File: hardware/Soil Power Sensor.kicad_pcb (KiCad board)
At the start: 2 copper layers, 139 x 45 mm, 72 parts, among them J1 Screw_Terminal_01x05, J2 RFShield_OnePiece, J3 Debug, J4 Conn_01x03, J5 Micro_SD_Card, J7 Conn_01x04_Socket, J8 Conn_01x10, J9 Rsense, Q1 BSS123, Q2 L8050QLT1G, Q3 L8050QLT1G, SW1 BOOT, SW2 EN, SW3 SW_SPDT, U1 MAX9944, U10 Wio-E5 mini, U11 MB85RC1MT, U12 MB85RC1MT, U2 INA296A, U3 REF2033, U4 THS4532, U5 TPS60400DBV, U6 ADS1219, U7 SN74LVC1G240, U8 ESP32-C3-WROOM-02-N4

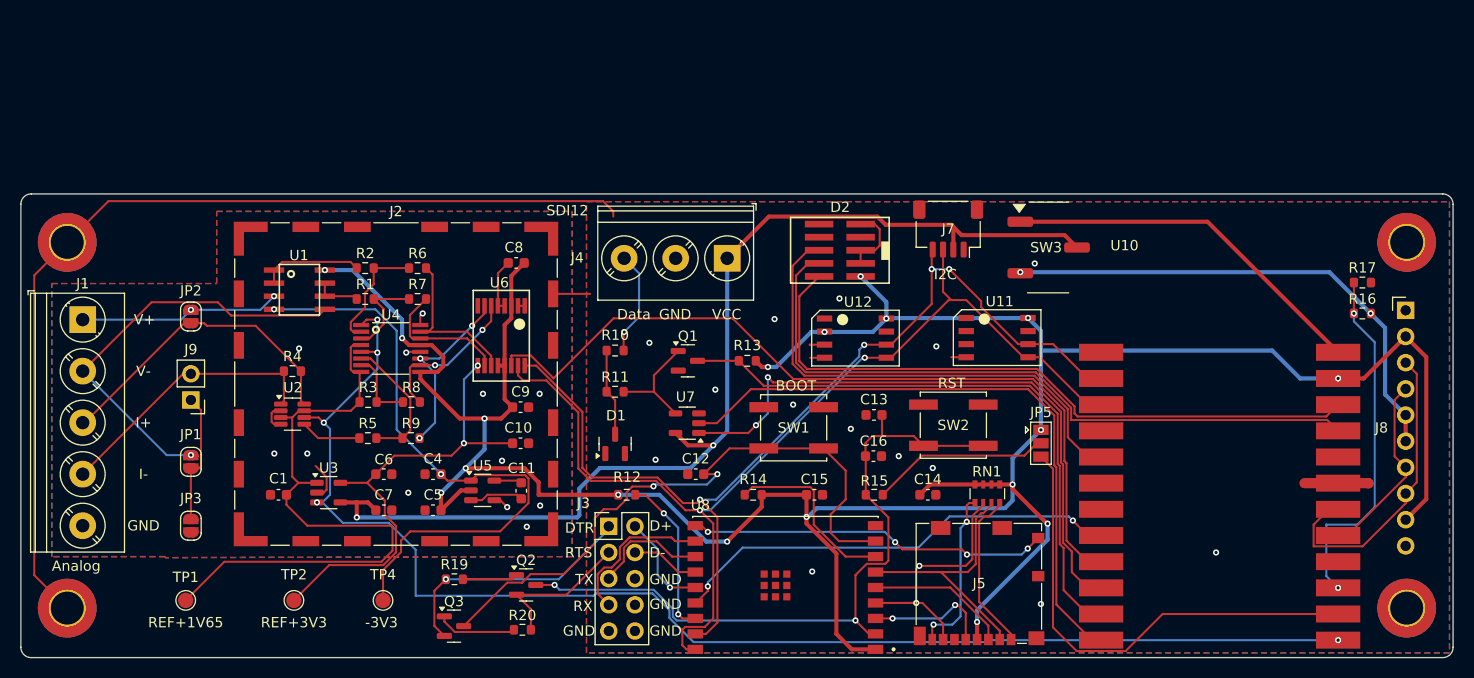
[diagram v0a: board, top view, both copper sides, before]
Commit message: replace mini with module
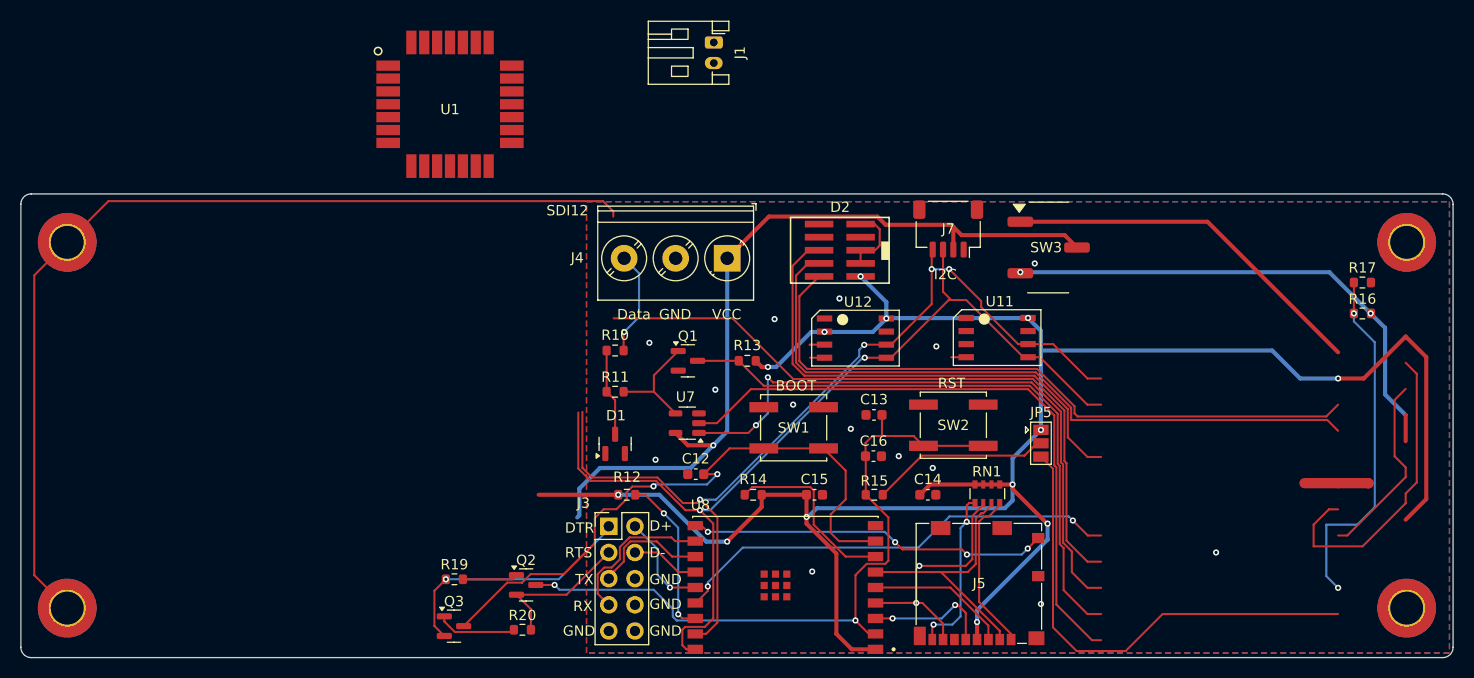
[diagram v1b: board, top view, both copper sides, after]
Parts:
- removed C1, C10, C6, C7, C8, C9: 0.1uF, Capacitor_SMD:C_0603_1608Metric
- removed C11, C4, C5: 1uF, Capacitor_SMD:C_0603_1608Metric
- removed J2: RFShield_OnePiece, RF_Shielding:Wuerth_36103305_30x30mm
- removed J8: Conn_01x10, Connector_PinHeader_2.54mm:PinHeader_1x10_P2.54mm_Horizontal
- removed J9: Rsense, Connector_PinHeader_2.54mm:PinHeader_1x02_P2.54mm_Vertical
- removed JP1, JP2, JP3: SolderJumper_2_Open, Jumper:SolderJumper-2_P1.3mm_Open_RoundedPad1.0x1.5mm
- removed R1, R2, R6, R7: 100k, Resistor_SMD:R_0603_1608Metric
- removed R3, R5: 10k, Resistor_SMD:R_0603_1608Metric
- removed R4: 330m, Resistor_SMD:R_0603_1608Metric
- removed R8, R9: 499k, Resistor_SMD:R_0603_1608Metric
- removed TP1: REF+1V65, TestPoint:TestPoint_Pad_D1.5mm
- removed TP2: REF+3V3, TestPoint:TestPoint_Pad_D1.5mm
- removed TP4: -3V3, TestPoint:TestPoint_Pad_D1.5mm
- removed U10: Wio-E5 mini, Soil Power Sensor:WIO-E5_MINI
- removed U2: INA296A, Package_TO_SOT_SMD:SOT-23-8
- removed U3: REF2033, Package_TO_SOT_SMD:SOT-23-5
- removed U4: THS4532, Soil Power Sensor:SOP65P640X120-16N
- removed U5: TPS60400DBV, Package_TO_SOT_SMD:SOT-23-5
- removed U6: ADS1219, Soil Power Sensor:TSSOP65P640X120-16
- J1: value Screw_Terminal_01x05 -> Conn_01x02; footprint TerminalBlock_Phoenix:TerminalBlock_Phoenix_PT-1,5-5-5.0-H_1x05_P5.00mm_Horizontal -> Connector_JST:JST_PH_S2B-PH-K_1x02_P2.00mm_Horizontal
- U1: value MAX9944 -> LoRa-E5; footprint Soil Power Sensor:SOIC127P600X155-8N -> Soil Power Sensor:LoRa-E5
- moved J1 66.9 mm to (179.2, 32.1)
- moved U1 23.2 mm to (153.7, 38.1)
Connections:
- J1 pad 1: /Analog/V+ -> /Power/VBAT
- J1 pad 2: /Analog/V- -> GND
- U1 pad 1: Net-(U1A--) -> +3V3
- U1 pad 2: Net-(U1A--) -> GND
- U1 pad 3: /Analog/V+ -> /STM32/STM_SWDIO
- U1 pad 4: -3V3 -> /STM32/STM_SWDCLK
- U1 pad 5: /Analog/V- -> unconnected-(U1-PB15-Pad5)
- U1 pad 6: Net-(U1B--) -> unconnected-(U1-PA15-Pad6)
- U1 pad 7: Net-(U1B--) -> unconnected-(U1-PB4-Pad7)
- U1 pad 8: +3V3 -> /STM32/STM_SWO
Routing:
- net /Analog/POWERDOWN: track 134.0 -> 0.00 mm, vias 5 -> 0
- net (no net): track 0.00 -> 113.0 mm
- net /Analog/ADC_DRDY: track 78.6 -> 0.00 mm
- net +3V3: track 279.8 -> 209.8 mm, vias 18 -> 13
- net REF+1V65: track 62.2 -> 0.00 mm
- net -3V3: track 60.4 -> 0.00 mm, vias 2 -> 0
- net REF+3V3: track 46.1 -> 0.00 mm, vias 2 -> 0
- net /Analog/V-: track 40.9 -> 0.00 mm, vias 1 -> 0
- net /Analog/I+: track 30.4 -> 0.00 mm
- net /Power/~{PG}: track 30.3 -> 0.00 mm
- net /Analog/I-: track 27.0 -> 0.00 mm
- net VCC: track 106.2 -> 79.6 mm, vias 2 -> 1
- net GND: track 131.5 -> 111.3 mm, vias 26 -> 14
- net /Analog/V+: track 19.5 -> 0.00 mm, vias 2 -> 0
- net /Power/~{CHG}: track 18.4 -> 0.00 mm
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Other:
- board text removed: "-3V3"
- board text removed: "Analog"
- board text removed: "I+"
- board text removed: "I-"
- board text removed: "REF+1V65"
- board text removed: "REF+3V3"
- board text removed: "V+"
- board text removed: "V-"

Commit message: john pcb review feedback
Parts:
- moved J1 8.33 mm to (171.7, 35.5)
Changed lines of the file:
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@@
 	(footprint "Connector_JST:JST_PH_S2B-PH-K_1x02_P2.00mm_Horizontal"
 		(layer "F.Cu")
-		(at 179.25 32.1 -90)
+		(at 171.65 35.5 -90)
 		(descr "JST PH series connector, S2B-PH-K (http://www.jst-mfg.com/product/pdf/eng/ePH.pdf), generated with kicad-footprint-generator")
 		(tags "connector JST PH horizontal")
@@
 			(type solid)
 		)
+	)
+	(gr_text_box "100 x 50 mm\nholes 5mm offset from corners\nholes 5mm offset from center sides"
+		(start 160 109.8)
+		(end 210.4 124.6)
+		(margins 1.0025 1.0025 1.0025 1.0025)
+		(layer "Cmts.User")
+		(effects
+			(font
+				(size 1.5 1.5)
+				(thickness 0.3)
+				(bold yes)
+			)
+			(justify left top)
+		)
+		(border yes)
+		(stroke
+			(width 0.2)
+			(type solid)
+		)

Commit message: pcb outline
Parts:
- removed SW1: BOOT, Button_Switch_SMD:SW_Push_1P1T_NO_CK_KSC7xxJ
- removed SW2: EN, Button_Switch_SMD:SW_Push_1P1T_NO_CK_KSC7xxJ
- removed U12: MB85RC1MT, Soil Power Sensor:SOP127P505X155-8N
- added C1: 1 uF, Capacitor_SMD:C_0603_1608Metric, F.Cu at (65.9, 67.8)
- added C10: 100nF, Capacitor_SMD:C_0603_1608Metric, F.Cu at (221.2, 150.0)
- added C11: 10uF, Capacitor_SMD:C_0603_1608Metric, F.Cu at (235.3, 128.3)
- added C17: 0.1uF, Capacitor_SMD:C_0603_1608Metric, F.Cu at (49.2, 67.8)
- added C18: 0.1uF, Capacitor_SMD:C_0603_1608Metric, F.Cu at (49.2, 70.3)
- added C19: 10uF, Capacitor_SMD:C_0603_1608Metric, F.Cu at (43.8, 42.4)
- added C2: 1 uF, Capacitor_SMD:C_0603_1608Metric, F.Cu at (65.9, 70.3)
- added C20: 0.1uF, Capacitor_SMD:C_0603_1608Metric, F.Cu at (43.8, 44.9)
- added C21: 47 uF, Capacitor_SMD:C_0603_1608Metric, F.Cu at (69.9, 70.3)
- added C3: 100nF, Capacitor_SMD:C_0603_1608Metric, F.Cu at (65.9, 72.8)
- added C4: 10uF, Capacitor_SMD:C_0603_1608Metric, F.Cu at (65.9, 75.4)
- added C5: 100nF, Capacitor_SMD:C_0603_1608Metric, F.Cu at (65.9, 77.9)
- added C6: 10uF, Capacitor_SMD:C_0603_1608Metric, F.Cu at (65.9, 80.4)
- added C7: 47 uF, Capacitor_SMD:C_0603_1608Metric, F.Cu at (69.9, 67.8)
- added C8: 0.1uF, Capacitor_SMD:C_0603_1608Metric, F.Cu at (43.8, 32.3)
- added C9: 0.1uF, Capacitor_SMD:C_0603_1608Metric, F.Cu at (43.8, 34.8)
- added D10: LED, LED_SMD:LED_0603_1608Metric, F.Cu at (229.2, 155.0)
- added D11: D, Diode_SMD:D_0603_1608Metric, F.Cu at (115.7, 34.0)
- added D12: D, Diode_SMD:D_0603_1608Metric, F.Cu at (115.7, 36.6)
- added D3: LED, LED_SMD:LED_0603_1608Metric, F.Cu at (70.3, 43.7)
- added D4: ARM10_DEBUG, Soil Power Sensor:ARM10_DEBUG, F.Cu at (34.0, 49.3)
- added D5: BZX84Cxx, Package_TO_SOT_SMD:SOT-23, F.Cu at (28.2, 50.3)
- added D6: ESD131-B1-W0201, Diode_SMD:Infineon_SG-WLL-2-3_0.58x0.28_P0.36mm, F.Cu at (224.1, 130.4)
- added D7: ESD131-B1-W0201, Diode_SMD:Infineon_SG-WLL-2-3_0.58x0.28_P0.36mm, F.Cu at (239.3, 152.0)
- added D8: ESD131-B1-W0201, Diode_SMD:Infineon_SG-WLL-2-3_0.58x0.28_P0.36mm, F.Cu at (237.8, 152.0)
- added D9: LED, LED_SMD:LED_0603_1608Metric, F.Cu at (229.2, 152.4)
- added F2: Fuse_Small, Fuse:Fuse_0603_1608Metric, F.Cu at (134.7, 33.0)
- added F3: Polyfuse, Fuse:Fuse_0603_1608Metric, F.Cu at (124.3, 34.0)
- added FL1: 0603USB-222, Inductor_SMD:L_CommonModeChoke_Coilcraft_0603USB, F.Cu at (238.5, 150.2)
- added J10: Conn_01x04_Socket, Connector_JST:JST_SH_SM04B-SRSS-TB_1x04-1MP_P1.00mm_Horizontal, F.Cu at (46.2, 52.4)
- added J11: Conn_01x04_Pin, Connector_PinHeader_2.54mm:PinHeader_1x04_P2.54mm_Vertical, F.Cu at (62.1, 20.1)
- added J12: Conn_01x04_Socket, Connector_JST:JST_SH_SM04B-SRSS-TB_1x04-1MP_P1.00mm_Horizontal, F.Cu at (46.2, 60.0)
- added J13: USB_C_Receptacle_USB2.0_16P, Connector_USB:USB_C_Receptacle_GCT_USB4110, F.Cu at (238.9, 158.1)
- added J15: Conn_01x03, Connector_PinHeader_2.54mm:PinHeader_1x03_P2.54mm_Vertical, F.Cu at (135.0, 22.4)
- added J16: Micro_SD_Card, Connector_Card:microSD_HC_Molex_104031-0811, F.Cu at (163.0, 143.4)
- added J2: DC050-T, Connector_BarrelJack:BarrelJack_Horizontal, F.Cu at (128.2, 25.4)
- added J6: SMA-K, Connector_Coaxial:SMA_Molex_73251-1153_EdgeMount_Horizontal, F.Cu at (56.6, 24.4)
- added J8: Conn_01x03, TerminalBlock_Phoenix:TerminalBlock_Phoenix_PT-1,5-3-5.0-H_1x03_P5.00mm_Horizontal, F.Cu at (57.3, 36.1)
- added J9: Conn_01x06_Pin, Connector_PinHeader_2.54mm:PinHeader_2x04_P2.54mm_Vertical, F.Cu at (56.1, 54.7)
- added JP1: Jumper_2_Bridged, Connector_PinHeader_2.54mm:PinHeader_1x02_P2.54mm_Vertical, F.Cu at (70.8, 83.9)
- added JP10: SolderJumper_2_Open, Jumper:SolderJumper-2_P1.3mm_Open_RoundedPad1.0x1.5mm, F.Cu at (27.9, 42.8)
- added JP11: SolderJumper_2_Open, Jumper:SolderJumper-2_P1.3mm_Open_RoundedPad1.0x1.5mm, F.Cu at (27.9, 46.3)
- added JP12: Jumper_3_Open, Connector_PinHeader_2.54mm:PinHeader_1x03_P2.54mm_Vertical, F.Cu at (66.2, 83.9)
- added JP13: Jumper_3_Open, Connector_PinHeader_2.54mm:PinHeader_1x03_P2.54mm_Vertical, F.Cu at (67.8, 54.7)
- added JP2: SolderJumper_2_Open, Jumper:SolderJumper-2_P1.3mm_Open_RoundedPad1.0x1.5mm, F.Cu at (82.1, 68.3)
- added JP3: SolderJumper_2_Open, Jumper:SolderJumper-2_P1.3mm_Open_RoundedPad1.0x1.5mm, F.Cu at (82.1, 71.9)
- added JP4: SolderJumper_2_Open, Jumper:SolderJumper-2_P1.3mm_Open_RoundedPad1.0x1.5mm, F.Cu at (82.1, 75.5)
- added JP6: SolderJumper_2_Open, Jumper:SolderJumper-2_P1.3mm_Open_RoundedPad1.0x1.5mm, F.Cu at (82.1, 79.0)
- added JP7: SolderJumper_2_Open, Jumper:SolderJumper-2_P1.3mm_Open_RoundedPad1.0x1.5mm, F.Cu at (27.9, 35.7)
- added JP8: Jumper_3_Open, Connector_PinHeader_2.54mm:PinHeader_1x03_P2.54mm_Vertical, F.Cu at (63.2, 54.7)
- added JP9: SolderJumper_2_Open, Jumper:SolderJumper-2_P1.3mm_Open_RoundedPad1.0x1.5mm, F.Cu at (27.9, 39.2)
- added L1: 1uH, Inductor_SMD:L_0805_2012Metric, F.Cu at (120.0, 34.1)
- added Q10: AO3401A, Package_TO_SOT_SMD:SOT-23, F.Cu at (86.8, 77.7)
- added Q6: AO3401A, Package_TO_SOT_SMD:SOT-23, F.Cu at (28.2, 54.8)
- added Q7: AO3401A, Package_TO_SOT_SMD:SOT-23, F.Cu at (28.2, 59.2)
- added Q8: AO3401A, Package_TO_SOT_SMD:SOT-23, F.Cu at (86.8, 68.8)
- added Q9: BSS123, Package_TO_SOT_SMD:SOT-23, F.Cu at (86.8, 73.2)
- added R1: 1M, Resistor_SMD:R_0603_1608Metric, F.Cu at (69.9, 72.8)
- added R18: 1k, Resistor_SMD:R_0603_1608Metric, F.Cu at (251.2, 152.0)
- added R2: 1M, Resistor_SMD:R_0603_1608Metric, F.Cu at (69.9, 75.4)
- added R21: 5.1k, Resistor_SMD:R_0603_1608Metric, F.Cu at (225.2, 147.5)
- added R22: 5.1k, Resistor_SMD:R_0603_1608Metric, F.Cu at (225.2, 150.0)
- added R23: 1k, Resistor_SMD:R_0603_1608Metric, F.Cu at (206.7, 146.0)
- added R24: 1k, Resistor_SMD:R_0603_1608Metric, F.Cu at (206.7, 148.5)
- added R26: 91k, Resistor_SMD:R_0603_1608Metric, F.Cu at (73.9, 77.9)
- added R27: 10k, Resistor_SMD:R_0603_1608Metric, F.Cu at (49.2, 72.8)
- added R28: 10k, Resistor_SMD:R_0603_1608Metric, F.Cu at (49.2, 75.4)
- added R29: 0, Resistor_SMD:R_0603_1608Metric, F.Cu at (49.2, 77.9)
- added R3: 2 kOhm, Resistor_SMD:R_0603_1608Metric, F.Cu at (69.9, 77.9)
- added R30: 0, Resistor_SMD:R_0603_1608Metric, F.Cu at (49.2, 80.4)
- added R31: 10k, Resistor_SMD:R_0603_1608Metric, F.Cu at (49.2, 82.9)
- added R34: 47k, Resistor_SMD:R_0603_1608Metric, F.Cu at (47.8, 44.9)
- added R35: 47k, Resistor_SMD:R_0603_1608Metric, F.Cu at (47.8, 47.4)
- added R36: 47k, Resistor_SMD:R_0603_1608Metric, F.Cu at (51.8, 32.3)
- added R37: 47k, Resistor_SMD:R_0603_1608Metric, F.Cu at (51.8, 34.8)
- added R38: 4.7k, Resistor_SMD:R_0603_1608Metric, F.Cu at (51.8, 37.3)
- added R39: 4.7k, Resistor_SMD:R_0603_1608Metric, F.Cu at (51.8, 39.9)
- added R4: 2 kOhm, Resistor_SMD:R_0603_1608Metric, F.Cu at (69.9, 80.4)
- added R40: 470k, Resistor_SMD:R_0603_1608Metric, F.Cu at (73.9, 80.4)
- added R41: 10k, Resistor_SMD:R_0603_1608Metric, F.Cu at (78.0, 67.8)
- added R42: 10k, Resistor_SMD:R_0603_1608Metric, F.Cu at (78.0, 70.3)
- added R43: 470k, Resistor_SMD:R_0603_1608Metric, F.Cu at (78.0, 72.8)
- added R44: 10k, Resistor_SMD:R_0603_1608Metric, F.Cu at (78.0, 75.4)
- added R45: 470k, Resistor_SMD:R_0603_1608Metric, F.Cu at (78.0, 77.9)
- added R5: 1 MOhm, Resistor_SMD:R_0603_1608Metric, F.Cu at (73.9, 67.8)
- added R6: 1 MOhm, Resistor_SMD:R_0603_1608Metric, F.Cu at (73.9, 70.3)
- added R7: 7.32 kOhm, Resistor_SMD:R_0603_1608Metric, F.Cu at (73.9, 72.8)
- added R8: 680 Ohm, Resistor_SMD:R_0603_1608Metric, F.Cu at (73.9, 75.4)
- added R9: 1k, Resistor_SMD:R_0603_1608Metric, F.Cu at (43.8, 47.4)
- added RT1: 21.5 kOhm, Resistor_SMD:R_0603_1608Metric, F.Cu at (78.0, 80.4)
- added SW4: BOOT/USER, Button_Switch_SMD:SW_Push_1P1T_NO_CK_KSC7xxJ, F.Cu at (35.7, 59.5)
- added SW5: BOOT, Button_Switch_SMD:SW_Push_1P1T_NO_CK_KSC7xxJ, F.Cu at (56.3, 70.5)
- added SW6: EN, Button_Switch_SMD:SW_Push_1P1T_NO_CK_KSC7xxJ, F.Cu at (56.3, 78.2)
- added TH1: 103AT NTC, Connector_PinHeader_2.54mm:PinHeader_1x02_P2.54mm_Vertical, F.Cu at (75.4, 83.9)
- added TP1: Vin, TestPoint:TestPoint_Pad_D1.5mm, F.Cu at (79.5, 83.4)
- added TP2: VBAT sense, TestPoint:TestPoint_Pad_D1.5mm, F.Cu at (79.5, 87.0)
- added U10: TCA9535PWR, Package_SO:TSSOP-24_4.4x7.8mm_P0.65mm, F.Cu at (34.8, 38.6)
- added U3: SN74LVC1G240, Package_TO_SOT_SMD:SOT-23-5, F.Cu at (32.6, 45.6)
- added U4: LoRa-E5, Soil Power Sensor:LoRa-E5, F.Cu at (188.8, 123.0)
- added U5: MB85RC1MT, Soil Power Sensor:SOP127P505X155-8N, F.Cu at (69.5, 21.3)
- added U6: MAX3072E, Package_SO:SOIC-8_3.9x4.9mm_P1.27mm, F.Cu at (68.6, 27.7)
- added U9: ESP32-C3-WROOM-02-N4, Soil Power Sensor:MODULE_ESP32-C3-WROOM-02-N4, F.Cu at (115.9, 122.8)
- C12: value 0.1uF -> 10uF
- C13: value 0.1uF -> 100nF
- D1: value BZX84Cxx -> LED; footprint Package_TO_SOT_SMD:SOT-23 -> LED_SMD:LED_0603_1608Metric
- D2: value ARM10_DEBUG -> LED; footprint Soil Power Sensor:ARM10_DEBUG -> LED_SMD:LED_0603_1608Metric
- J3: value Debug -> Conn_01x10_Pin; footprint Connector_PinHeader_2.54mm:PinHeader_2x05_P2.54mm_Vertical -> Connector_PinHeader_2.54mm:PinHeader_1x10_P2.54mm_Vertical
- J5: value Micro_SD_Card -> AudioJack3; footprint Connector_Card:microSD_HC_Molex_104031-0811 -> Connector_Audio:Jack_3.5mm_CUI_SJ-3523-SMT_Horizontal
- J7: value Conn_01x04_Socket -> U-FL; footprint Connector_JST:JST_SH_SM04B-SRSS-TB_1x04-1MP_P1.00mm_Horizontal -> Connector_Coaxial:U.FL_Hirose_U.FL-R-SMT-1_Vertical
- JP5: value ESP_EN -> SolderJumper_2_Bridged; footprint Jumper:SolderJumper-3_P1.3mm_Open_Pad1.0x1.5mm -> Jumper:SolderJumper-2_P1.3mm_Bridged_RoundedPad1.0x1.5mm
- Q2, Q3: value L8050QLT1G -> AO3401A
- R12: value 10k -> 47k
- R13: value 47k -> 0
- R14, R15: value 10k -> 0
- R16, R17: value 1M -> 0
- R19, R20: value 10k -> 20
- SW3: value SW_SPDT -> RST; footprint Soil Power Sensor:JS102011SCQN -> Button_Switch_SMD:SW_Push_1P1T_NO_CK_KSC7xxJ
- U1: value LoRa-E5 -> BQ24210DQCR
- U11: value MB85RC1MT -> TPS631000DRLR; footprint Soil Power Sensor:SOP127P505X155-8N -> Soil Power Sensor:TPS631000DRLR_TEX
- U7: value SN74LVC1G240 -> MB85RC1MT; footprint Package_TO_SOT_SMD:SOT-23-5 -> Soil Power Sensor:SOP127P505X155-8N
- U8: value ESP32-C3-WROOM-02-N4 -> CP2102N-Axx-xQFN24; footprint Soil Power Sensor:MODULE_ESP32-C3-WROOM-02-N4 -> Package_DFN_QFN:QFN-24-1EP_4x4mm_P0.5mm_EP2.6x2.6mm
- moved C13 135.8 mm to (306.2, 145.9)
- moved R19 109.9 mm to (247.5, 142.0), turned to 90 degrees
- moved R20 103.4 mm to (249.5, 142.0), turned to 90 degrees
- moved J3 84.6 mm to (87.0, 99.5)
- moved C12 84.2 mm to (243.8, 126.0)
- moved U8 78.0 mm to (238.5, 146.0), turned to 90 degrees
- moved H4 77.6 mm to (195.0, 145.0)
- moved R17 75.6 mm to (244.8, 131.0)
- moved H3 74.3 mm to (195.0, 105.0)
- moved H2 59.1 mm to (105.0, 145.0)
- moved H1 54.7 mm to (105.0, 105.0)
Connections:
- C12 pad 1: /ESP32/BOOT -> /Power/VUSB
- C13 pad 1: /ESP32/EN -> Net-(U8-~{DTR})
- C13 pad 2: GND -> /STM32/RST
- D1 pad 1: GND -> Net-(D1-K)
- D1 pad 2: unconnected-(D1-NC-Pad2) -> Net-(D1-A)
- D2 pad 1: +3V3 -> Net-(D2-K)
- D2 pad 2: /STM32/STM_SWDIO -> Net-(D2-A)
- J3 pad 1: /ESP32/DTR -> unconnected-(J3-Pin_1-Pad1)
- J3 pad 10: GND -> unconnected-(J3-Pin_10-Pad10)
- J3 pad 2: /ESP32/USB_D+ -> unconnected-(J3-Pin_2-Pad2)
- J3 pad 3: /ESP32/RTS -> unconnected-(J3-Pin_3-Pad3)
- J3 pad 4: /ESP32/USB_D- -> unconnected-(J3-Pin_4-Pad4)
- J3 pad 5: /ESP32/TX -> unconnected-(J3-Pin_5-Pad5)
- J3 pad 6: GND -> unconnected-(J3-Pin_6-Pad6)
- J3 pad 7: /ESP32/RX -> unconnected-(J3-Pin_7-Pad7)
- J3 pad 8: GND -> unconnected-(J3-Pin_8-Pad8)
- J3 pad 9: GND -> unconnected-(J3-Pin_9-Pad9)
- J4 pad 1: VCC -> SDI-12 VCC
- J7 pad 1: GND -> Net-(J7-In)
- J7 pad 2: VCC -> GND
- JP5 pad 1: +3V3 -> /Power/~{PG}
- JP5 pad 2: Net-(JP5-C) -> Net-(JP5-B)
- Q2 pad 1: Net-(Q2-B) -> Net-(J10-Pin_2)
- Q2 pad 2: /ESP32/RTS -> Net-(Q2-G)
- Q2 pad 3: /ESP32/EN -> +3V3
- Q3 pad 1: Net-(Q3-B) -> Net-(J12-Pin_2)
- Q3 pad 2: /ESP32/DTR -> Net-(Q3-G)
- Q3 pad 3: /ESP32/BOOT -> +3V3
- R10 pad 1: Net-(J4-Pin_3) -> Net-(JP13-A)
- R10 pad 2: Net-(D1-K) -> Net-(D5-K)
- R11 pad 1: Net-(D1-K) -> Net-(D5-K)
- R12 pad 1: Net-(U8-IO2) -> +3V3
- R12 pad 2: +3V3 -> /STM32/SDI12_RX
- R13 pad 1: +3V3 -> GND
- R13 pad 2: /STM32/SDI12_RX -> Net-(R13-Pad2)
- R14 pad 1: Net-(U8-IO8) -> Net-(C9-Pad1)
- R14 pad 2: +3V3 -> Net-(J6-In)
- R15 pad 1: Net-(JP5-C) -> Net-(U4-RFIO)
- R15 pad 2: /ESP32/EN -> Net-(C9-Pad1)
- R16 pad 1: /Power/VBAT -> Net-(C9-Pad1)
- R16 pad 2: /Power/VBAT/2 -> Net-(J7-In)
- R17 pad 1: /Power/VBAT/2 -> /Power/VUSB
- R17 pad 2: GND -> Net-(U8-VREGIN)
- R19 pad 1: /ESP32/DTR -> Net-(U8-TXD)
- R19 pad 2: Net-(Q2-B) -> /STM32/USART2_RX
- R20 pad 1: /ESP32/RTS -> Net-(U8-RXD)
- R20 pad 2: Net-(Q3-B) -> /STM32/USART2_TX
- RN1 pad 1: Net-(J5-DAT1) -> Net-(J16-DAT1)
- RN1 pad 4: Net-(J5-DAT2) -> Net-(J16-DAT2)
- SW3 pad 1: /Power/VUSB -> /STM32/RST
- SW3 pad 2: VCC -> GND
- U1 pad 1: +3V3 -> Net-(D11-K)
- U1 pad 10: unconnected-(U1-PB6-Pad10) -> Net-(JP6-B)
- U1 pad 11: unconnected-(U1-PB5-Pad11) -> 0
- U1 pad 12: /STM32/SDI12_TX -> (no net)
- U1 pad 13: unconnected-(U1-PC0-Pad13) -> (no net)
- U1 pad 14: GND -> (no net)
- U1 pad 15: unconnected-(U1-RFIO-Pad15) -> (no net)
- U1 pad 16: GND -> (no net)
- U1 pad 17: unconnected-(U1-RST-Pad17) -> (no net)
- U1 pad 18: unconnected-(U1-PA3-Pad18) -> (no net)
- U1 pad 19: unconnected-(U1-PA2-Pad19) -> (no net)
- U1 pad 2: GND -> Net-(U1-ISET)
- U1 pad 20: unconnected-(U1-PB10-Pad20) -> (no net)
- U1 pad 21: unconnected-(U1-PA9-Pad21) -> (no net)
- U1 pad 22: GND -> (no net)
- U1 pad 23: unconnected-(U1-PA0-Pad23) -> (no net)
- U1 pad 24: unconnected-(U1-PB13~{}-Pad24) -> (no net)
- U1 pad 25: unconnected-(U1-PB9-Pad25) -> (no net)
- U1 pad 26: unconnected-(U1-PB14-Pad26) -> (no net)
- U1 pad 27: unconnected-(U1-PA10-Pad27) -> (no net)
- U1 pad 28: unconnected-(U1-PB0-Pad28) -> (no net)
- U1 pad 3: /STM32/STM_SWDIO -> 0
- U1 pad 4: /STM32/STM_SWDCLK -> Net-(U1-VTSB)
- U1 pad 5: unconnected-(U1-PB15-Pad5) -> Net-(U1-TS)
- U1 pad 6: unconnected-(U1-PA15-Pad6) -> /Power/~{PG}
- U1 pad 7: unconnected-(U1-PB4-Pad7) -> Net-(JP5-B)
- U1 pad 8: /STM32/STM_SWO -> /Power/~{CHG}
- U1 pad 9: unconnected-(U1-PB7-Pad9) -> Net-(U1-VDPM)
- U11 pad 1: unconnected-(U11-NC-Pad1) -> Net-(JP1-A)
- U11 pad 2: unconnected-(U11-A1-Pad2) -> Net-(U11-LX2)
- U11 pad 3: unconnected-(U11-A2-Pad3) -> Net-(U11-LX1)
- U11 pad 4: GND -> Net-(D12-K)
- U11 pad 5: /STM32/SDA -> unconnected-(U11-EN-Pad5)
- U11 pad 6: /STM32/SCL -> unconnected-(U11-MODE-Pad6)
- U11 pad 7: unconnected-(U11-WP-Pad7) -> GND
- U11 pad 8: +3V3 -> Net-(U11-FB)
- U7 pad 1: /STM32/SDI12_DIR -> unconnected-(U7-NC-Pad1)
- U7 pad 2: /STM32/SDI12_TX -> +3V3
- U7 pad 4: Net-(Q1-G) -> GND
- U7 pad 5: VCC -> /STM32/SDA
- U8 pad 1: +3V3 -> unconnected-(U8-~{RI}/CLK-Pad1)
- U8 pad 10: /ESP32/CD -> unconnected-(U8-NC-Pad10)
- U8 pad 11: /ESP32/RX -> unconnected-(U8-~{WAKEUP}/GPIO.3-Pad11)
- U8 pad 12: /ESP32/TX -> unconnected-(U8-RS485/GPIO.2-Pad12)
- U8 pad 13: /ESP32/USB_D- -> Net-(D10-K)
- U8 pad 14: /ESP32/USB_D+ -> Net-(D9-K)
- U8 pad 15: /ESP32/WAKEUP -> unconnected-(U8-~{SUSPEND}-Pad15)
- U8 pad 16: Net-(U8-IO2) -> unconnected-(U8-NC-Pad16)
- U8 pad 17: /STM32/SCL -> unconnected-(U8-SUSPEND-Pad17)
- U8 pad 18: /STM32/SDA -> unconnected-(U8-~{CTS}-Pad18)
- U8 pad 2: /ESP32/EN -> GND
- U8 pad 3: /ESP32/CLK -> Net-(U8-D+)
- U8 pad 4: /ESP32/SDO -> Net-(U8-D-)
- U8 pad 5: /ESP32/SDI -> +3V3
- U8 pad 6: /ESP32/CS -> +3V3
- U8 pad 7: Net-(U8-IO8) -> Net-(U8-VREGIN)
- U8 pad 8: /ESP32/BOOT -> /Power/VUSB
- U8 pad 9: GND -> Net-(U8-~{RST})
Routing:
- net (no net): track 113.0 -> 375.0 mm, vias 0 -> 1
- net VCC: track 79.6 -> 0.00 mm, vias 1 -> 0
- net +3V3: track 209.8 -> 285.8 mm, vias 13 -> 17
- net /STM32/STM_SWDCLK: track 67.2 -> 0.00 mm
- net /STM32/RST: track 0.00 -> 66.4 mm
- net /STM32/STM_SWDIO: track 64.4 -> 0.00 mm
- net GND: track 111.3 -> 172.4 mm
- net /STM32/SDI12_TX: track 61.1 -> 0.00 mm
- net /STM32/SDI12_DIR: track 60.3 -> 0.00 mm, vias 2 -> 0
- net /STM32/STM_SWO: track 48.0 -> 0.00 mm
- net /Power/VUSB: track 36.1 -> 0.00 mm
- net Net-(J7-In): track 0.00 -> 34.6 mm, vias 0 -> 2
- net /Power/VBAT/2: track 34.6 -> 0.00 mm, vias 2 -> 0
- net Net-(Q3-G): track 0.00 -> 24.5 mm, vias 0 -> 1
- net /ESP32/DTR: track 24.5 -> 0.00 mm, vias 1 -> 0
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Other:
- board size 139 x 45 mm -> 151 x 103.2 mm

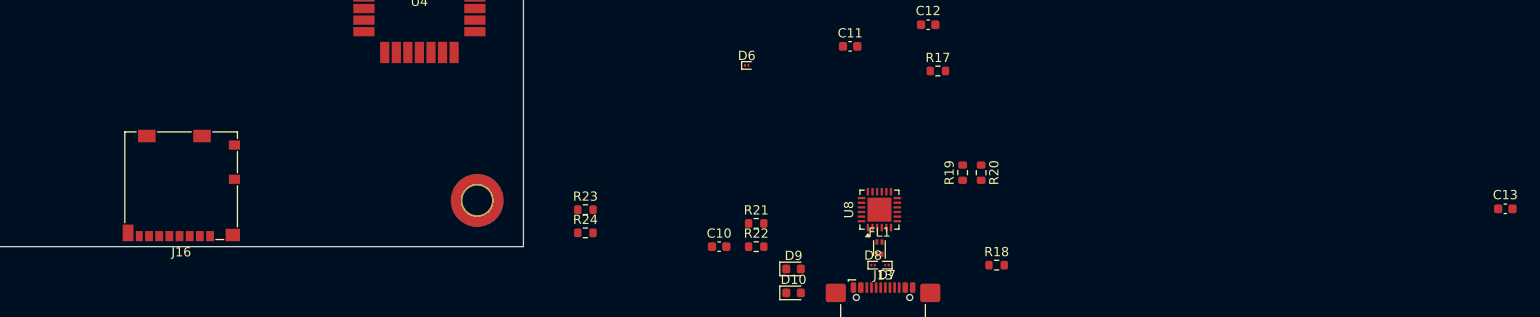
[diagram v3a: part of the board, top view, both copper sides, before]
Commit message: pin numbering and changed mosfets
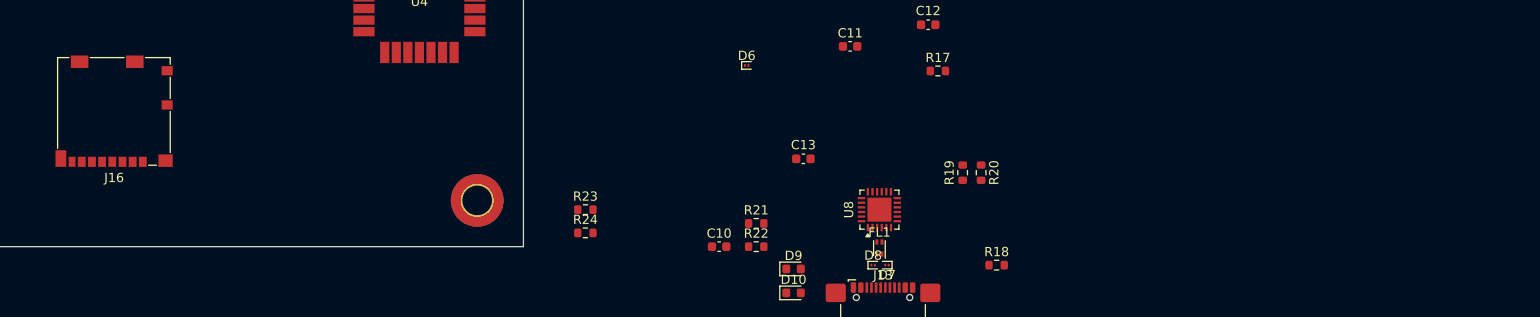
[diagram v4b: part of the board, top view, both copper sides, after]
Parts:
- moved C13 76.1 mm to (230.3, 140.5)
- moved J16 10.8 mm to (155.7, 135.4)
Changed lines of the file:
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@@
 	(footprint "Capacitor_SMD:C_0603_1608Metric"
 		(layer "F.Cu")
-		(at 306.191739 145.91 180)
+		(at 230.275 140.5 180)
 		(descr "Capacitor SMD 0603 (1608 Metric), square (rectangular) end terminal, IPC_7351 nominal, (Body size source: IPC-SM-782 page 76, https://www.pcb-3d.com/wordpress/wp-content/uploads/ipc-sm-782a_amendment_1_and_2.pdf), generated with kicad-footprint-generator")
 		(tags "capacitor")
@@
 	(footprint "Connector_Card:microSD_HC_Molex_104031-0811"
 		(layer "F.Cu")
-		(at 163 143.4125 180)
+		(at 155.73 135.375 180)
 		(descr "1.10mm Pitch microSD Memory Card Connector, Surface Mount, Push-Pull Type, 1.42mm Height, with Detect Switch (https://www.molex.com/pdm_docs/sd/1040310811_sd.pdf)")
 		(tags "microSD SD molex")

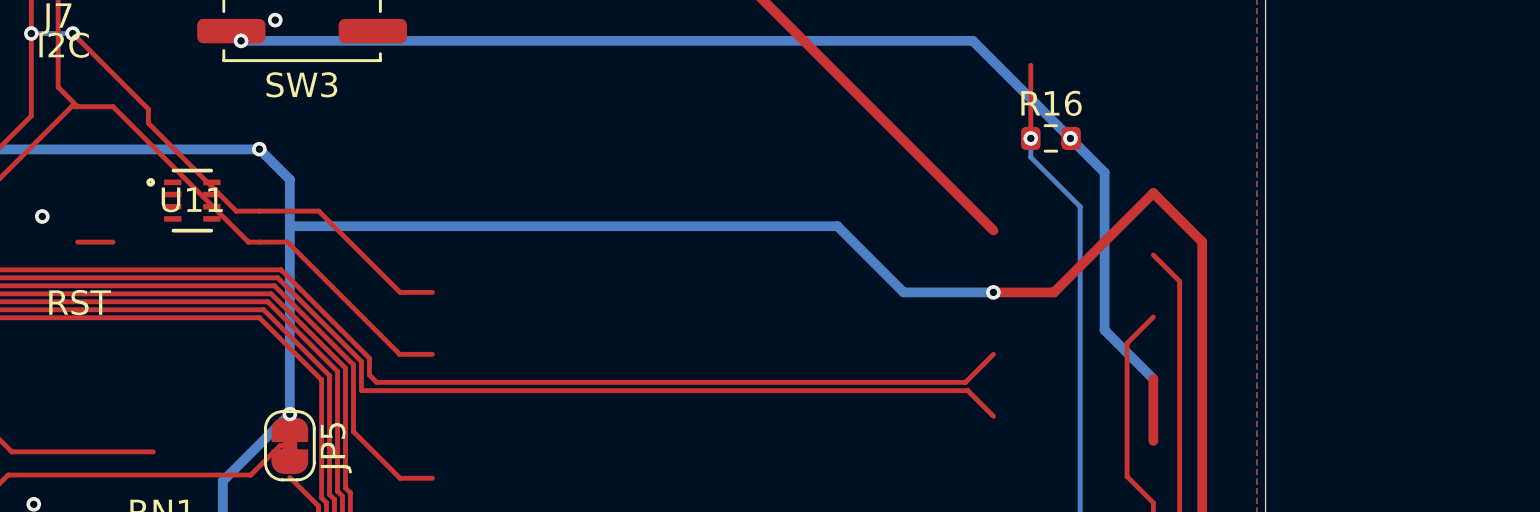
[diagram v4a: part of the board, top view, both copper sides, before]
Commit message: lower power buck-boost
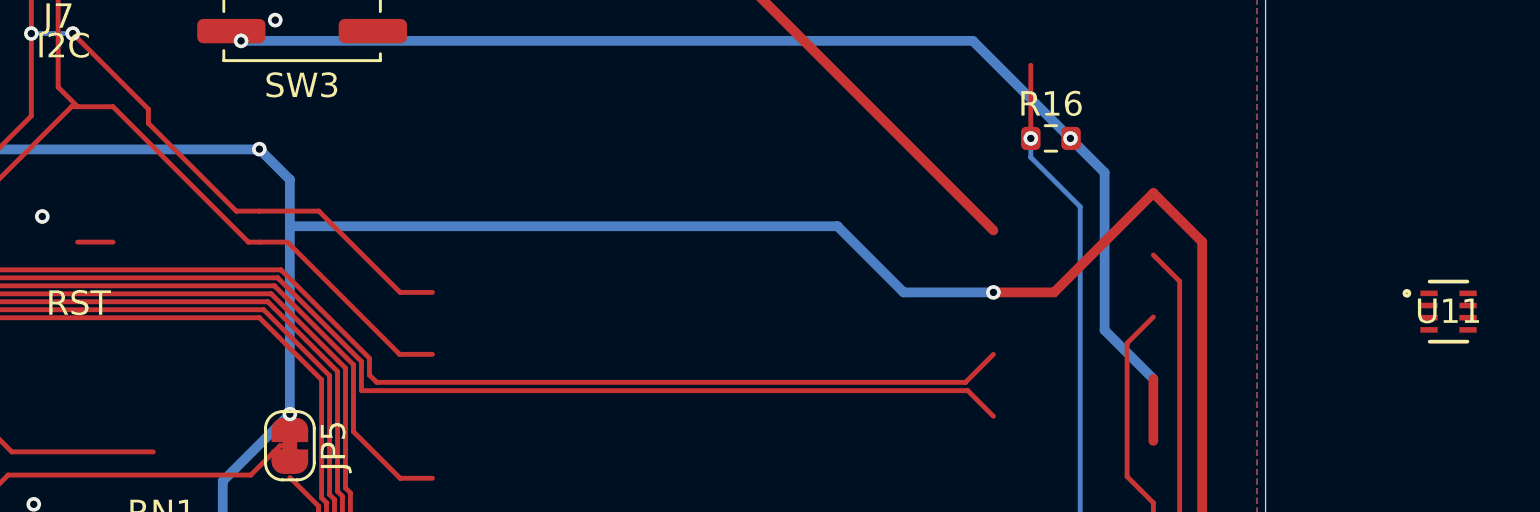
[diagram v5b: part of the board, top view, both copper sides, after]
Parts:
- moved U11 51.7 mm to (258.5, 65.5)
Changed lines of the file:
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@@
 	(footprint "Soil Power Sensor:TPS631000DRLR_TEX"
 		(layer "F.Cu")
-		(at 207 60.95)
+		(at 258.5 65.5)
 		(tags "TPS631000DRLR ")
 		(property "Reference" "U11"
